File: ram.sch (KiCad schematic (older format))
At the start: 31 parts, among them U16 NEC_424260, U17 NEC_424260, U18 NEC_424260, U19 NEC_424260, U32 74LS139, U34 74LS373, U35 74LS244

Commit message: Add video power
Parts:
- renumbered C4 to C994
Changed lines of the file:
@@
 	15240 7060 15240 7180
 $Comp
-L Device:C C4
+L Device:C C994
 U 1 1 5C78DDA4
 P 14930 3670
-F 0 "C4" H 14970 3770 50  0000 L CNN
+F 0 "C994" H 14970 3770 50  0000 L CNN
 F 1 "100n" H 14970 3580 50  0000 L CNN
 F 2 "" H 14968 3520 50  0001 C CNN

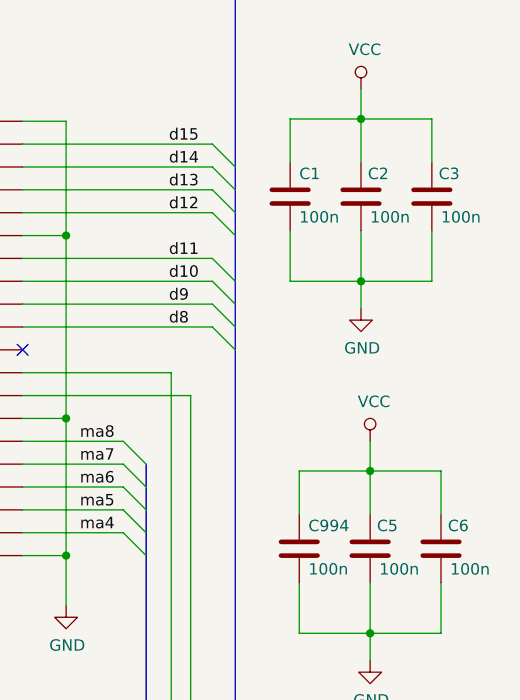
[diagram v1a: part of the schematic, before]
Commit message: Add expansion bus
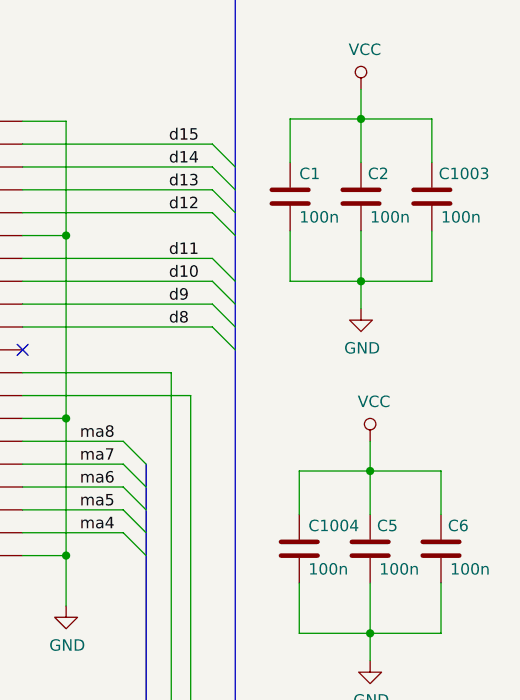
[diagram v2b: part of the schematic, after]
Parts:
- renumbered C3 to C1003, C994 to C1004
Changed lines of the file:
@@
 $Descr A3 16535 11693
 encoding utf-8
-Sheet 3 10
+Sheet 3 11
 Title "Rämixx500"
 Date "2019-04-20"
@@
 	15240 7060 15240 7180
 $Comp
-L Device:C C994
+L Device:C C1004
 U 1 1 5C78DDA4
 P 14930 3670
-F 0 "C994" H 14970 3770 50  0000 L CNN
+F 0 "C1004" H 14970 3770 50  0000 L CNN
 F 1 "100n" H 14970 3580 50  0000 L CNN
 F 2 "" H 14968 3520 50  0001 C CNN
@@
 $EndComp
 $Comp
-L Device:C C3
+L Device:C C1003
 U 1 1 5D2CAF4D
 P 15510 2130
-F 0 "C3" H 15540 2230 50  0000 L CNN
+F 0 "C1003" H 15540 2230 50  0000 L CNN
 F 1 "100n" H 15550 2040 50  0000 L CNN
 F 2 "" H 15548 1980 50  0001 C CNN

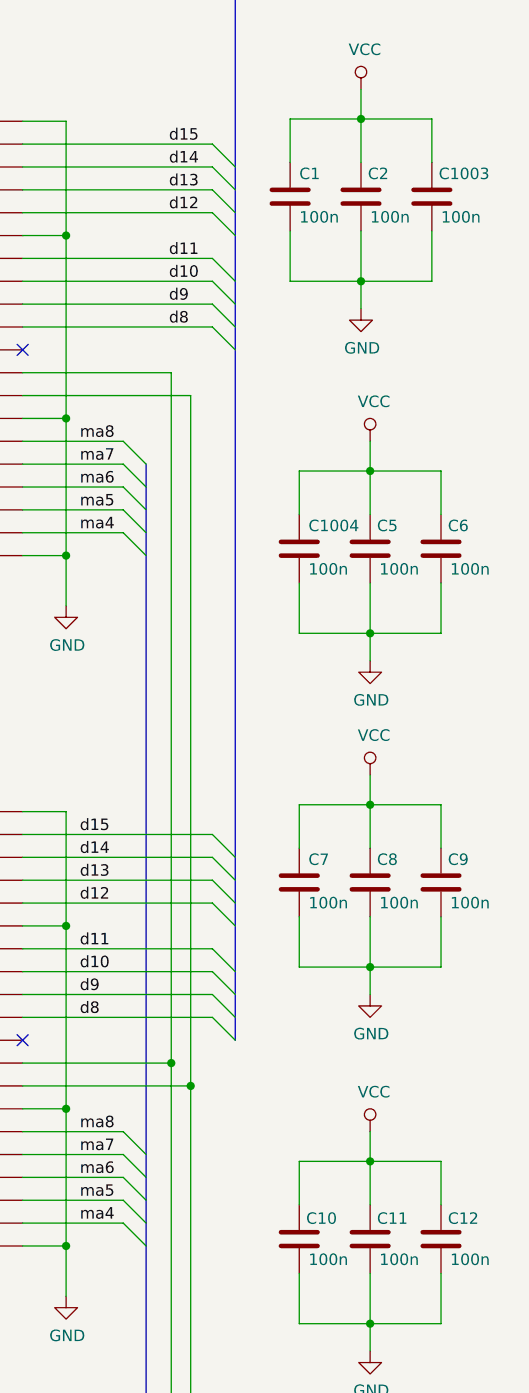
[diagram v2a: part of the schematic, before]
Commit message: Add power & decoupling, not yet complete
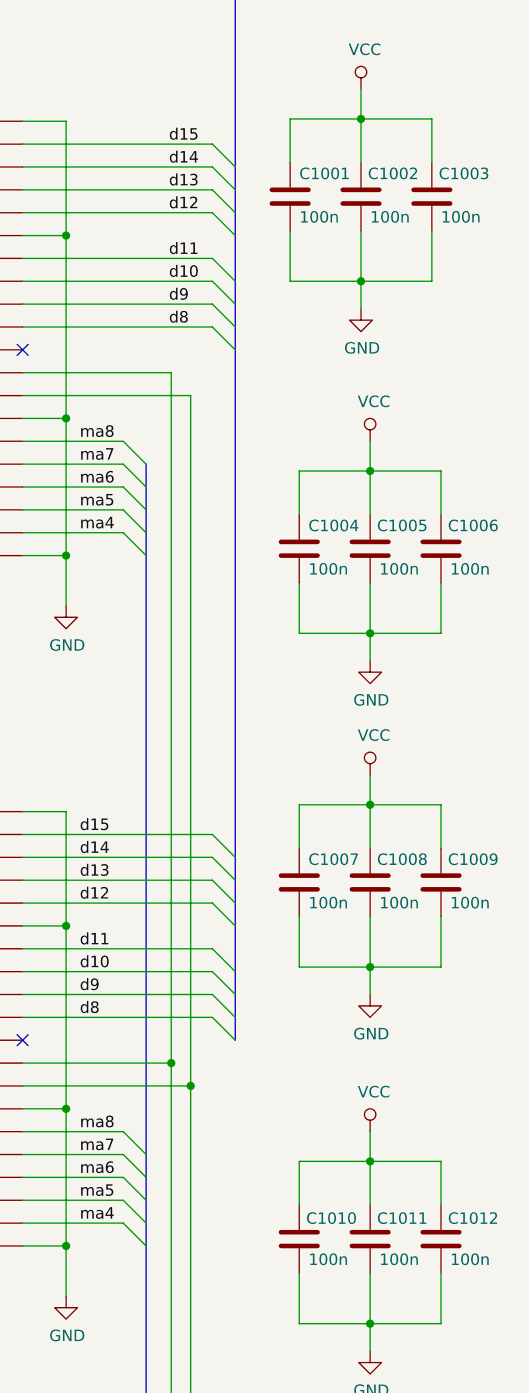
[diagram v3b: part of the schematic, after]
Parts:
- renumbered C1 to C1001, C2 to C1002, C5 to C1005, C6 to C1006, C7 to C1007, C8 to C1008, C9 to C1009, C10 to C1010, C11 to C1011, C12 to C1012
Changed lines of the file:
@@
 $Descr A3 16535 11693
 encoding utf-8
-Sheet 3 11
+Sheet 3 12
 Title "Rämixx500"
 Date "2019-04-20"
@@
 	11790 7895 14260 7895
 $Comp
-L Device:C C10
+L Device:C C1010
 U 1 1 5C6C8DDB
 P 14930 6690
-F 0 "C10" H 14960 6780 50  0000 L CNN
+F 0 "C1010" H 14960 6780 50  0000 L CNN
 F 1 "100n" H 14970 6600 50  0000 L CNN
 F 2 "" H 14968 6540 50  0001 C CNN
@@
 $EndComp
 $Comp
-L Device:C C11
+L Device:C C1011
 U 1 1 5C6C8E89
 P 15240 6690
-F 0 "C11" H 15270 6780 50  0000 L CNN
+F 0 "C1011" H 15270 6780 50  0000 L CNN
 F 1 "100n" H 15280 6600 50  0000 L CNN
 F 2 "" H 15278 6540 50  0001 C CNN
@@
 $EndComp
 $Comp
-L Device:C C12
+L Device:C C1012
 U 1 1 5C6C8F65
 P 15550 6690
-F 0 "C12" H 15580 6780 50  0000 L CNN
+F 0 "C1012" H 15580 6780 50  0000 L CNN
 F 1 "100n" H 15590 6600 50  0000 L CNN
 F 2 "" H 15588 6540 50  0001 C CNN
@@
 $EndComp
 $Comp
-L Device:C C5
+L Device:C C1005
 U 1 1 5C78DDAA
 P 15240 3670
-F 0 "C5" H 15270 3770 50  0000 L CNN
+F 0 "C1005" H 15270 3770 50  0000 L CNN
 F 1 "100n" H 15280 3580 50  0000 L CNN
 F 2 "" H 15278 3520 50  0001 C CNN
@@
 $EndComp
 $Comp
-L Device:C C6
+L Device:C C1006
 U 1 1 5C78DDB0
 P 15550 3670
-F 0 "C6" H 15580 3770 50  0000 L CNN
+F 0 "C1006" H 15580 3770 50  0000 L CNN
 F 1 "100n" H 15590 3580 50  0000 L CNN
 F 2 "" H 15588 3520 50  0001 C CNN
@@
 	8370 7895 10840 7895
 $Comp
-L Device:C C7
+L Device:C C1007
 U 1 1 5D288D48
 P 14930 5130
-F 0 "C7" H 14970 5230 50  0000 L CNN
+F 0 "C1007" H 14970 5230 50  0000 L CNN
 F 1 "100n" H 14970 5040 50  0000 L CNN
 F 2 "" H 14968 4980 50  0001 C CNN
@@
 $EndComp
 $Comp
-L Device:C C8
+L Device:C C1008
 U 1 1 5D288D4E
 P 15240 5130
-F 0 "C8" H 15270 5230 50  0000 L CNN
+F 0 "C1008" H 15270 5230 50  0000 L CNN
 F 1 "100n" H 15280 5040 50  0000 L CNN
 F 2 "" H 15278 4980 50  0001 C CNN
@@
 $EndComp
 $Comp
-L Device:C C9
+L Device:C C1009
 U 1 1 5D288D54
 P 15550 5130
-F 0 "C9" H 15580 5230 50  0000 L CNN
+F 0 "C1009" H 15580 5230 50  0000 L CNN
 F 1 "100n" H 15590 5040 50  0000 L CNN
 F 2 "" H 15588 4980 50  0001 C CNN
@@
 	15240 5500 15240 5620
 $Comp
-L Device:C C1
+L Device:C C1001
 U 1 1 5D2CAF41
 P 14890 2130
-F 0 "C1" H 14930 2230 50  0000 L CNN
+F 0 "C1001" H 14930 2230 50  0000 L CNN
 F 1 "100n" H 14930 2040 50  0000 L CNN
 F 2 "" H 14928 1980 50  0001 C CNN
@@
 $EndComp
 $Comp
-L Device:C C2
+L Device:C C1002
 U 1 1 5D2CAF47
 P 15200 2130
-F 0 "C2" H 15230 2230 50  0000 L CNN
+F 0 "C1002" H 15230 2230 50  0000 L CNN
 F 1 "100n" H 15240 2040 50  0000 L CNN
 F 2 "" H 15238 1980 50  0001 C CNN

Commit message: Add RTC
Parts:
- JP3A1, JP3B1, JP4A1, JP4B1: footprint Jumper:SolderJumper-2_P1.3mm_Bridged_RoundedPad1.0x1.5mm -> Raemixx500:Jumper2-Bridged
- JP5A1, JP5B1: footprint Jumper:SolderJumper-2_P1.3mm_Open_Pad1.0x1.5mm -> Raemixx500:Jumper2-Bridged
- R201, R202: footprint (none) -> Raemixx500:R_Axial_DIN0309_L9.0mm_D3.2mm_P12.70mm_Horizontal
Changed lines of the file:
@@
 $Descr A3 16535 11693
 encoding utf-8
-Sheet 3 12
+Sheet 3 13
 Title "Rämixx500"
 Date "2019-04-20"
@@
 F 0 "JP3A1" H 4850 5060 50  0000 C CNN
 F 1 "Jumper_2_Bridged" H 4850 5084 50  0001 C CNN
-F 2 "Jumper:SolderJumper-2_P1.3mm_Bridged_RoundedPad1.0x1.5mm" H 4850 4980 50  0001 C CNN
+F 2 "Raemixx500:Jumper2-Bridged" H 4850 4980 50  0001 C CNN
 F 3 "~" H 4850 4980 50  0001 C CNN
 	1    4850 4980
@@
 F 0 "JP3B1" H 4850 5105 50  0000 C CNN
 F 1 "Jumper_2_Bridged" H 4850 5294 50  0001 C CNN
-F 2 "Jumper:SolderJumper-2_P1.3mm_Bridged_RoundedPad1.0x1.5mm" H 4850 5190 50  0001 C CNN
+F 2 "Raemixx500:Jumper2-Bridged" H 4850 5190 50  0001 C CNN
 F 3 "~" H 4850 5190 50  0001 C CNN
 	1    4850 5190
@@
 F 0 "R201" V 6385 5105 50  0000 L CNN
 F 1 "4.7k" V 6475 5125 50  0000 L CNN
-F 2 "" V 6400 5205 50  0001 C CNN
+F 2 "Raemixx500:R_Axial_DIN0309_L9.0mm_D3.2mm_P12.70mm_Horizontal" V 6400 5205 50  0001 C CNN
 F 3 "~" H 6470 5205 50  0001 C CNN
 	1    6470 5205
@@
 F 0 "R202" V 6625 5110 50  0000 L CNN
 F 1 "4.7k" V 6715 5125 50  0000 L CNN
-F 2 "" V 6640 5205 50  0001 C CNN
+F 2 "Raemixx500:R_Axial_DIN0309_L9.0mm_D3.2mm_P12.70mm_Horizontal" V 6640 5205 50  0001 C CNN
 F 3 "~" H 6710 5205 50  0001 C CNN
 	1    6710 5205
@@
 F 0 "JP4B1" H 6315 7635 50  0000 C CNN
 F 1 "Jumper_2_Bridged" H 6315 7824 50  0001 C CNN
-F 2 "Jumper:SolderJumper-2_P1.3mm_Bridged_RoundedPad1.0x1.5mm" H 6315 7720 50  0001 C CNN
+F 2 "Raemixx500:Jumper2-Bridged" H 6315 7720 50  0001 C CNN
 F 3 "~" H 6315 7720 50  0001 C CNN
 	1    6315 7720
@@
 F 0 "JP4A1" H 6315 7385 50  0000 C CNN
 F 1 "Jumper_2_Bridged" H 6315 7574 50  0001 C CNN
-F 2 "Jumper:SolderJumper-2_P1.3mm_Bridged_RoundedPad1.0x1.5mm" H 6315 7470 50  0001 C CNN
+F 2 "Raemixx500:Jumper2-Bridged" H 6315 7470 50  0001 C CNN
 F 3 "~" H 6315 7470 50  0001 C CNN
 	1    6315 7470
@@
 F 0 "JP5B1" H 6315 8425 50  0000 C CNN
 F 1 "Jumper_2_Bridged" H 6315 8614 50  0001 C CNN
-F 2 "Jumper:SolderJumper-2_P1.3mm_Open_Pad1.0x1.5mm" H 6315 8510 50  0001 C CNN
+F 2 "Raemixx500:Jumper2-Bridged" H 6315 8510 50  0001 C CNN
 F 3 "~" H 6315 8510 50  0001 C CNN
 	1    6315 8510
@@
 F 0 "JP5A1" H 6315 8175 50  0000 C CNN
 F 1 "Jumper_2_Bridged" H 6315 8364 50  0001 C CNN
-F 2 "Jumper:SolderJumper-2_P1.3mm_Open_Pad1.0x1.5mm" H 6315 8260 50  0001 C CNN
+F 2 "Raemixx500:Jumper2-Bridged" H 6315 8260 50  0001 C CNN
 F 3 "~" H 6315 8260 50  0001 C CNN
 	1    6315 8260

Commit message: Replace RAM with original design
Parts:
- removed C1001, C1002, C1003, C1004, C1005, C1006, C1007, C1008, C1009, C1010, C1011, C1012: 100n, symbol Device:C
- removed JP4A1, JP4B1, JP5A1, JP5B1: Jumper_2_Bridged, Raemixx500:Jumper2-Bridged, symbol Jumper:Jumper_2_Bridged
- removed RP999: 68, Resistor_THT:R_Array_SIP10, symbol Device:R_Pack05_SIP
- removed U16, U17, U18, U19: NEC_424260, symbol NEC_424260:NEC_424260
- added JPA4, JPB4: Jumper_3_Open, Raemixx500:Jumper3-Open, symbol Jumper:Jumper_3_Open
- added U16, U17, U18, U19, U20, U21, U22, U23: XX4256, Package_DIP:DIP-20_W7.62mm_Socket_LongPads, symbol XX4256:XX4256
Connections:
- net GND: now also U16.16 (~OE), U17.16 (~OE), U18.16 (~OE), U19.16 (~OE), U20.16 (~OE), U21.16 (~OE), U22.16 (~OE), U23.16 (~OE)
- net d0: now also U16.18 (D3), U20.18 (D3)
- net d1: now also U16.2 (D2), U20.2 (D2)
- net d10: now also U18.19 (D4), U22.19 (D4)
- net d11: now also U18.1 (D1), U22.1 (D1)
- net d12: now also U19.18 (D3), U23.18 (D3)
- net d13: now also U19.2 (D2), U23.2 (D2)
- net d14: now also U19.19 (D4), U23.19 (D4)
- net d15: now also U19.1 (D1), U23.1 (D1)
- net d2: now also U16.19 (D4), U20.19 (D4)
- net d3: now also U16.1 (D1), U20.1 (D1)
- net d4: now also U17.18 (D3), U21.18 (D3)
- net d5: now also U17.2 (D2), U21.2 (D2)
- net d6: now also U17.19 (D4), U21.19 (D4)
- net d7: now also U17.1 (D1), U21.1 (D1)
- net d8: now also U18.18 (D3), U22.18 (D3)
- net d9: now also U18.2 (D2), U22.2 (D2)
- net ma0: now also U16.6 (A0), U17.6 (A0), U18.6 (A0), U19.6 (A0), U20.6 (A0), U21.6 (A0), U22.6 (A0), U23.6 (A0)
- net ma1: now also U16.7 (A1), U17.7 (A1), U18.7 (A1), U19.7 (A1), U20.7 (A1), U21.7 (A1), U22.7 (A1), U23.7 (A1)
- net ma2: now also U16.8 (A2), U17.8 (A2), U18.8 (A2), U19.8 (A2), U20.8 (A2), U21.8 (A2), U22.8 (A2), U23.8 (A2)
- net ma3: now also U16.9 (A3), U17.9 (A3), U18.9 (A3), U19.9 (A3), U20.9 (A3), U21.9 (A3), U22.9 (A3), U23.9 (A3)
- net ma4: now also U16.11 (A4), U17.11 (A4), U18.11 (A4), U19.11 (A4), U20.11 (A4), U21.11 (A4), U22.11 (A4), U23.11 (A4)
- net ma5: now also RP201.8 (R4.2), U16.12 (A5), U17.12 (A5), U18.12 (A5), U19.12 (A5), U20.12 (A5), U21.12 (A5), U22.12 (A5), U23.12 (A5)
- net ma6: now also U16.13 (A6), U17.13 (A6), U18.13 (A6), U19.13 (A6), U20.13 (A6), U21.13 (A6), U22.13 (A6), U23.13 (A6)
- net ma7: now also U16.14 (A7), U17.14 (A7), U18.14 (A7), U19.14 (A7), U20.14 (A7), U21.14 (A7), U22.14 (A7), U23.14 (A7)
- net ma8: now also U16.15 (A8), U17.15 (A8), U18.15 (A8), U19.15 (A8), U20.15 (A8), U21.15 (A8), U22.15 (A8), U23.15 (A8)
- net ~bcasl0: now also JPA4.1 (A)
- net ~bcasu0: now also JPB4.1 (A)
- net at R201.2, RP203.2 (R1.2): now also U16.4 (~RAS), U16.5 (NC), U17.4 (~RAS), U17.5 (NC), U18.4 (~RAS), U18.5 (NC), U19.4 (~RAS), U19.5 (NC), U20.5 (NC), U21.5 (NC), U22.5 (NC), U23.5 (NC)
- net at R202.2, RP203.4 (R2.2): now also U20.4 (~RAS), U21.4 (~RAS), U22.4 (~RAS), U23.4 (~RAS)
- net at RP203.10 (R5.2): now also U16.3 (~WE), U17.3 (~WE), U18.3 (~WE), U19.3 (~WE), U20.3 (~WE), U21.3 (~WE), U22.3 (~WE), U23.3 (~WE)
- net at RP203.6 (R3.2): now also U18.17 (~CAS), U22.17 (~CAS), U23.17 (~CAS)
- net at RP203.8 (R4.2): now also U16.17 (~CAS), U17.17 (~CAS), U20.17 (~CAS), U21.17 (~CAS)
- net at U35.12 (O3a): now also JPB4.2 (C)
- net at U35.14 (O2a): now also JPA4.2 (C)
- net ~bcasl1 renamed ~BCASL1
- net ~BCASL1: now also JPA4.3 (B)
- net ~bcasu1 renamed ~BCASU1
- net ~BCASU1: now also JPB4.3 (B)
- no-connect marks 28 -> 6
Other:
- note added: "Note: JP4 bypasses\nU32 for 512K system"
- note added: "Note: U20-23, U23 not loaded for 512K system"
- note removed: ""EXTERNAL" RAM\n(~CAS1~)"
- note removed: ""INTERNAL" RAM\n(~CAS0~)"
- note removed: "JP4 and JP5 swap "internal"\nand "external" banks"
- note removed: "Not in original\nschematics"
- note removed: "Output pins 12 and 14 are only\nused on 512K systems so we don't\nneed them. Maybe use them to\nbuffer ~casu and ~casl?"
- note removed: "SPARES"
- note removed: "TBD: Power for all 74xx"
